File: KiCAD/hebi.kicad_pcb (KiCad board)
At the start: 4 copper layers, 49 x 49 mm, 111 parts, among them K1 CONN_3, K2 CONN_3, K3 CONN_3, K4 CONN_3, K5 CONN_3, P1 CONN_4, P2 CONN_4, P3 CONN_4, P4 CONN_4, P5 CONN_2, P6 CONN_2, Q1 MOS_N_DIODE, Q10 MOS_N_DIODE, Q2 MOS_N_DIODE, Q3 MOS_N_DIODE, Q4 MOS_N_DIODE, Q5 MOS_N_DIODE, Q6 MOS_N_DIODE, Q7 MOS_N_DIODE, Q8 MOS_N, Q9 MOS_N_DIODE, SW1 SW_PUSH, SW2 SW_PUSH, SW3 SW_PUSH, U1 MPU-6050, U2 HMC5883L, U3 MCP1825S, U4 STM32F407VG, U5 XBEE, U6 74AHC2G126, X1 8MHz

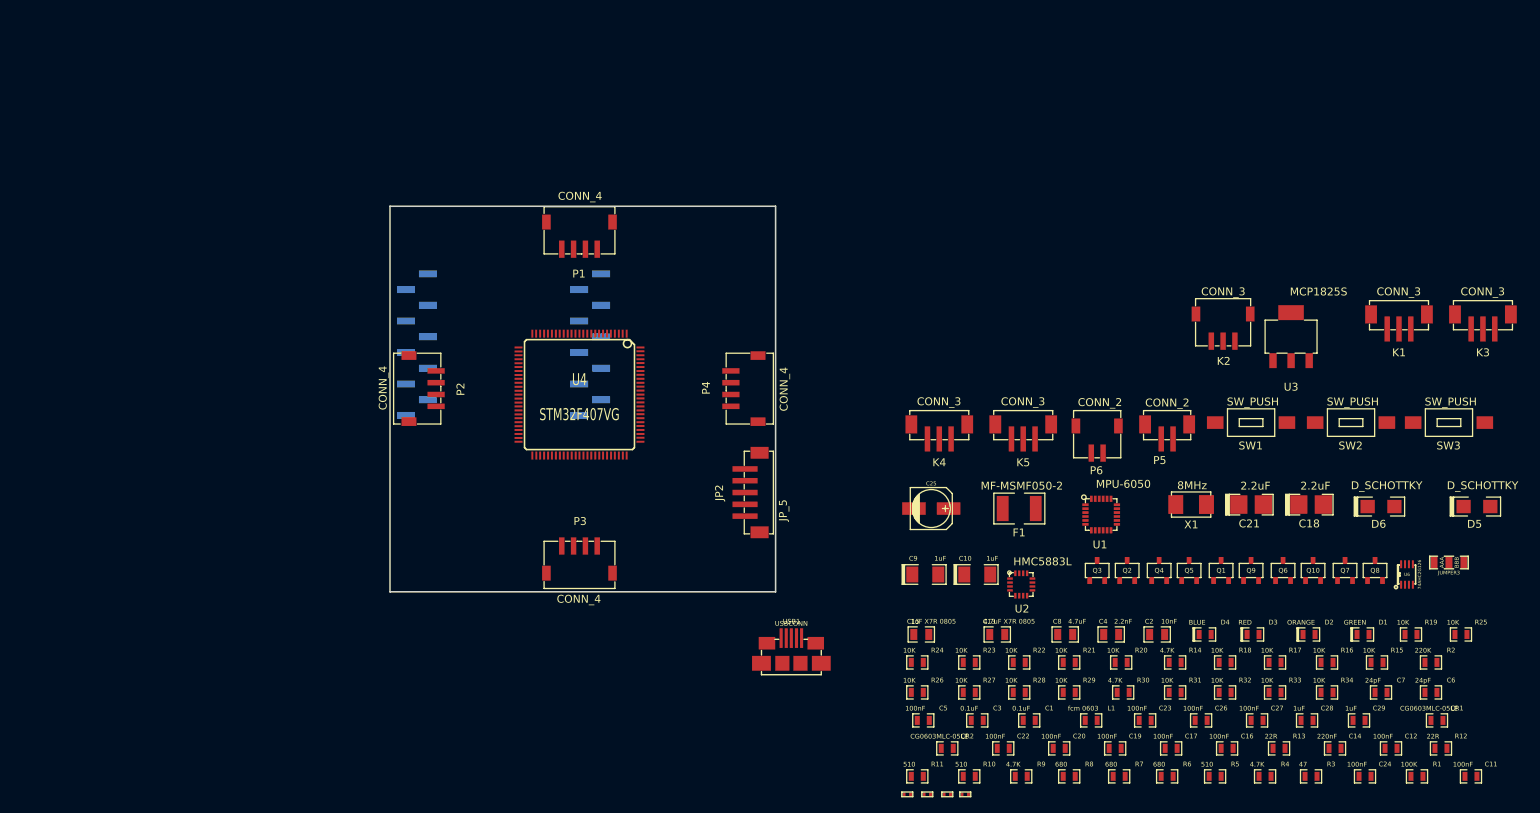
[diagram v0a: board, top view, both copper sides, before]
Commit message: Placed some components on the PCB.
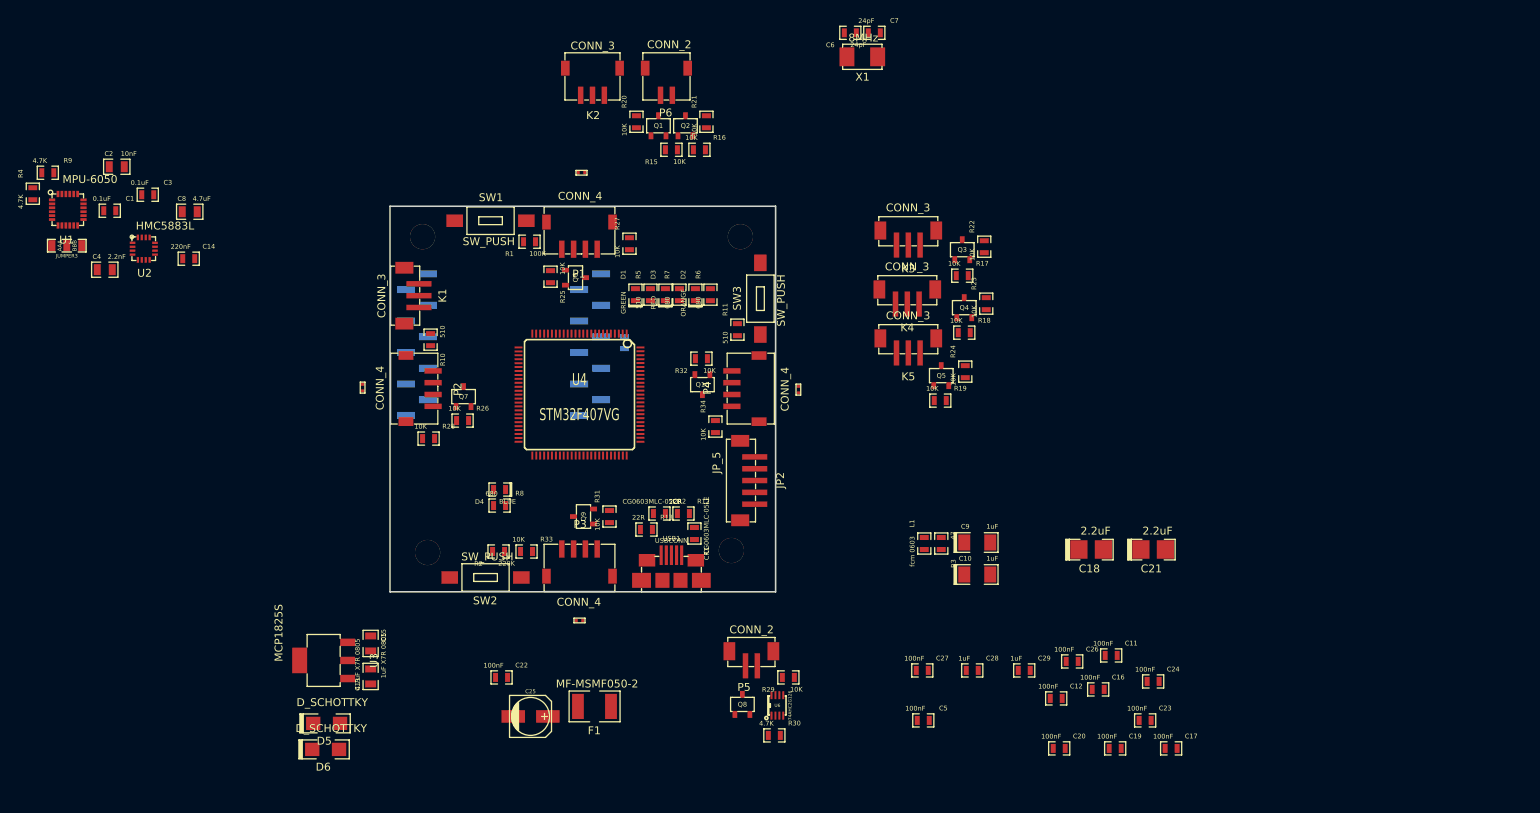
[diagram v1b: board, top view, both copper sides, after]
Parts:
- added Taladro3mm: 3mm, Taladro3mm, F.Cu at (178.6, 155.7)
- added Taladro3mm: 3mm, Taladro3mm, F.Cu at (217.2, 155.4)
- added Taladro3mm: 3mm, Taladro3mm, F.Cu at (177.9, 115.6)
- added Taladro3mm: 3mm, Taladro3mm, F.Cu at (218.3, 115.6)
- Q1, Q10, Q2, Q3, Q4, Q5, Q6, Q7, Q8, Q9: footprint SMT4dummies_SOT23-5_Opendous -> hebi_SOT23-3
- R14: moved to B.Cu
- moved JP1 180.2 mm to (132.7, 116.7)
- moved R4 173.2 mm to (128.4, 110.1), turned to 90 degrees
- moved C14 158.4 mm to (148.2, 118.4)
- moved D5 148.8 mm to (165.7, 177.4)
- moved R9 145.6 mm to (130.3, 107.4)
- moved C2 145.0 mm to (139.1, 106.7)
- moved D6 137.6 mm to (165.6, 180.7)
- moved U1 136.9 mm to (132.8, 112.1)
- moved C4 136.0 mm to (137.5, 119.8)
- moved C1 133.6 mm to (138.2, 112.3)
- moved R1 131.7 mm to (191.5, 116.2), turned to 180 degrees
- moved U3 129.6 mm to (165.4, 169.4), turned to 90 degrees
- moved K1 128.1 mm to (173.9, 123.1), turned to 90 degrees
- moved C3 124.8 mm to (143.0, 110.2)
- moved R25 124.3 mm to (194.2, 120.7), turned to 270 degrees
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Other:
- net class Thin added: clearance 0.254, trace_width 0.2, via_dia 0.889, via_drill 0.635
- rule trace_min: 0.254 -> 0.1524

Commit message: Placed more footprints on board.
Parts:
- K2, P6, Q1, Q2, R15, R16, R20, R21: moved to B.Cu
- moved R6 32.2 mm to (240.0, 142.6)
- moved D1 32.2 mm to (230.5, 142.6)
- moved D2 32.2 mm to (238.1, 142.6)
- moved D3 32.2 mm to (234.3, 142.6)
- moved R5 32.2 mm to (232.4, 142.6)
- moved R7 32.2 mm to (236.1, 142.6)
- moved R20 22.5 mm to (217.0, 120.0)
- moved R21 20.7 mm to (206.0, 120.0)
- moved Q1 20.0 mm to (214.1, 120.5), turned to 180 degrees
- moved R15 20.0 mm to (214.2, 124.0)
- moved K2 19.9 mm to (202.6, 111.9), turned to 180 degrees
- moved R16 19.9 mm to (209.0, 124.0), turned to 180 degrees
- moved P6 19.8 mm to (211.5, 111.9), turned to 180 degrees
- moved Q2 19.2 mm to (209.0, 120.5), turned to 180 degrees
- moved U5 13.7 mm to (198.1, 138.7)
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
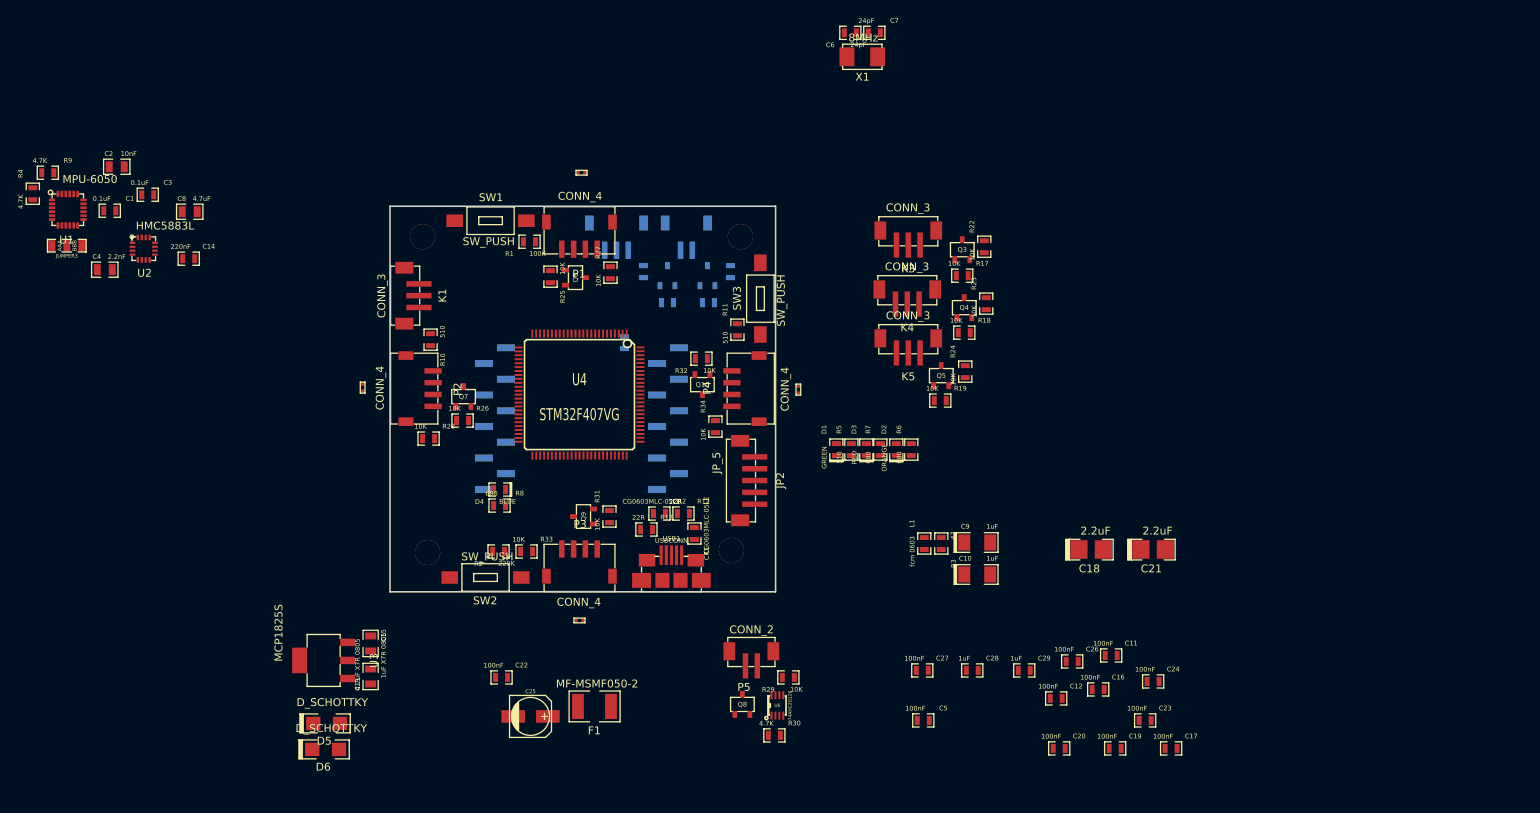
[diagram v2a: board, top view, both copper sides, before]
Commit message: Removed dynamixel due to spatial requirements (no space left for that)
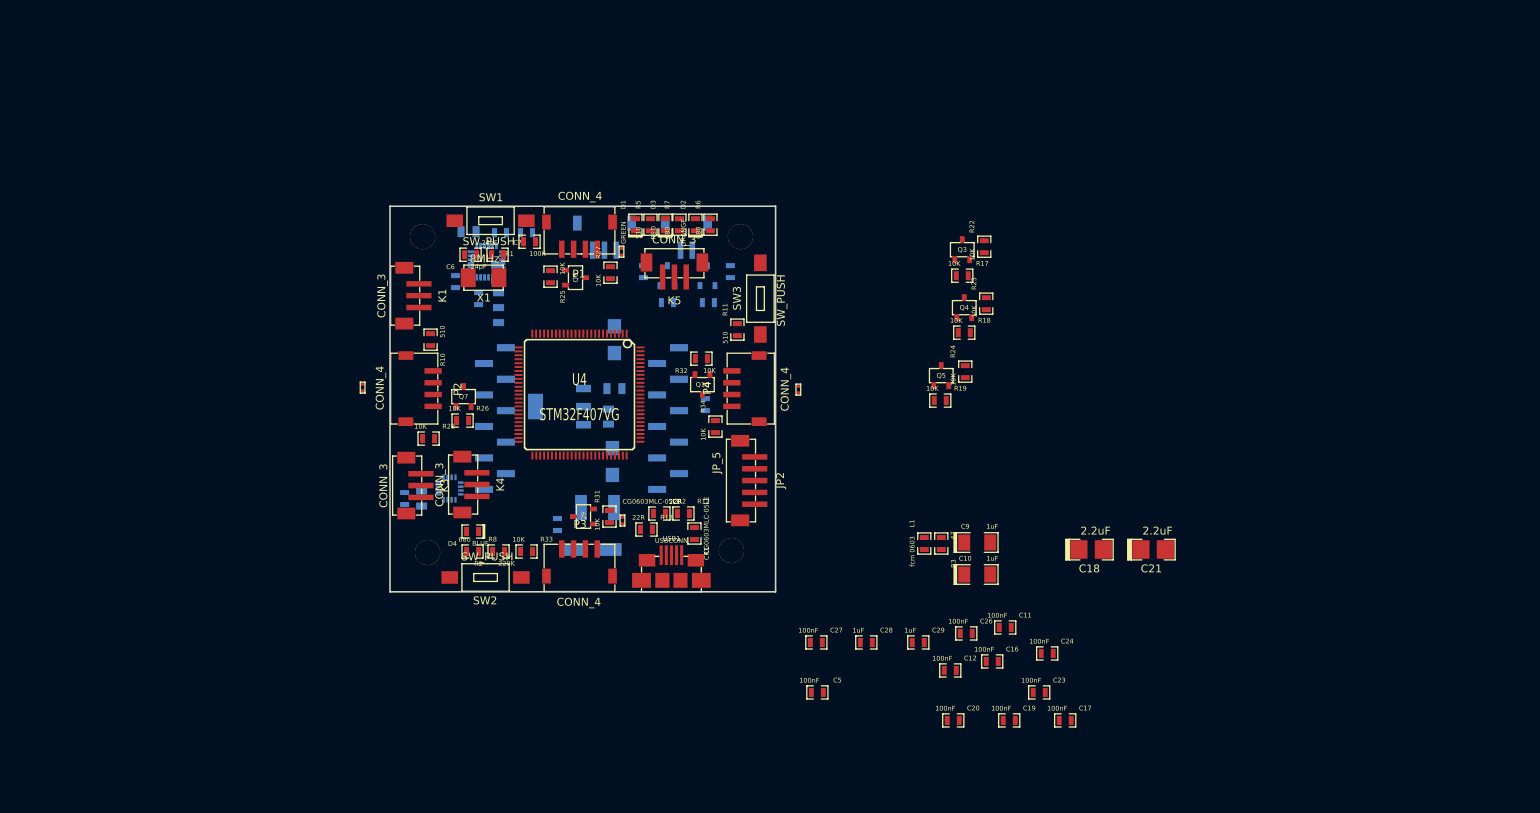
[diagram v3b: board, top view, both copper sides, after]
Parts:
- removed P5: CONN_2, ZH_CONN_B2B-ZR-SM4-TF
- removed Q8: MOS_N, hebi_SOT23-3
- removed R29: 10K, SM0603_Opendous(generic)
- removed R30: 4.7K, SM0603_Opendous(generic)
- removed U6: 74AHC2G126, VSSOP8_0.5mmPitch_2.3mm
- C1, C13, C14, C15, C2, C22, C25, C3, C4, C8, D5, D6, F1, JP1, R4, R9, U1, U2, U3: moved to B.Cu
- moved K3 73.9 mm to (174.1, 147.2), turned to 90 degrees
- moved K4 64.1 mm to (181.2, 147.1), turned to 90 degrees
- moved R4 62.9 mm to (191.1, 115.1), turned to 0 degrees
- moved D5 61.0 mm to (202.3, 128.7), turned to 90 degrees
- moved R9 58.0 mm to (187.8, 115.1), turned to 180 degrees
- moved C6 55.9 mm to (184.0, 117.9)
- moved X1 55.7 mm to (185.7, 120.8)
- moved C7 55.6 mm to (187.5, 117.9)
- moved JP1 55.4 mm to (187.6, 124.6), turned to 270 degrees
- moved U1 53.6 mm to (186.1, 118.7), turned to 180 degrees
- moved D6 51.6 mm to (202.1, 144.1), turned to 270 degrees
- moved C2 50.1 mm to (187.3, 120.1), turned to 90 degrees
- moved U2 49.4 mm to (181.4, 147.6), turned to 180 degrees
- moved C13 47.9 mm to (202.3, 134.9), turned to 0 degrees
- moved C8 46.9 mm to (177.8, 148.8), turned to 270 degrees
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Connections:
- U4 pad 80: /TX_DYN -> N-0000072
- U4 pad 82: /DIR_PORT_DYN -> N-0000070
- U4 pad 83: /RX_DYN -> N-0000071

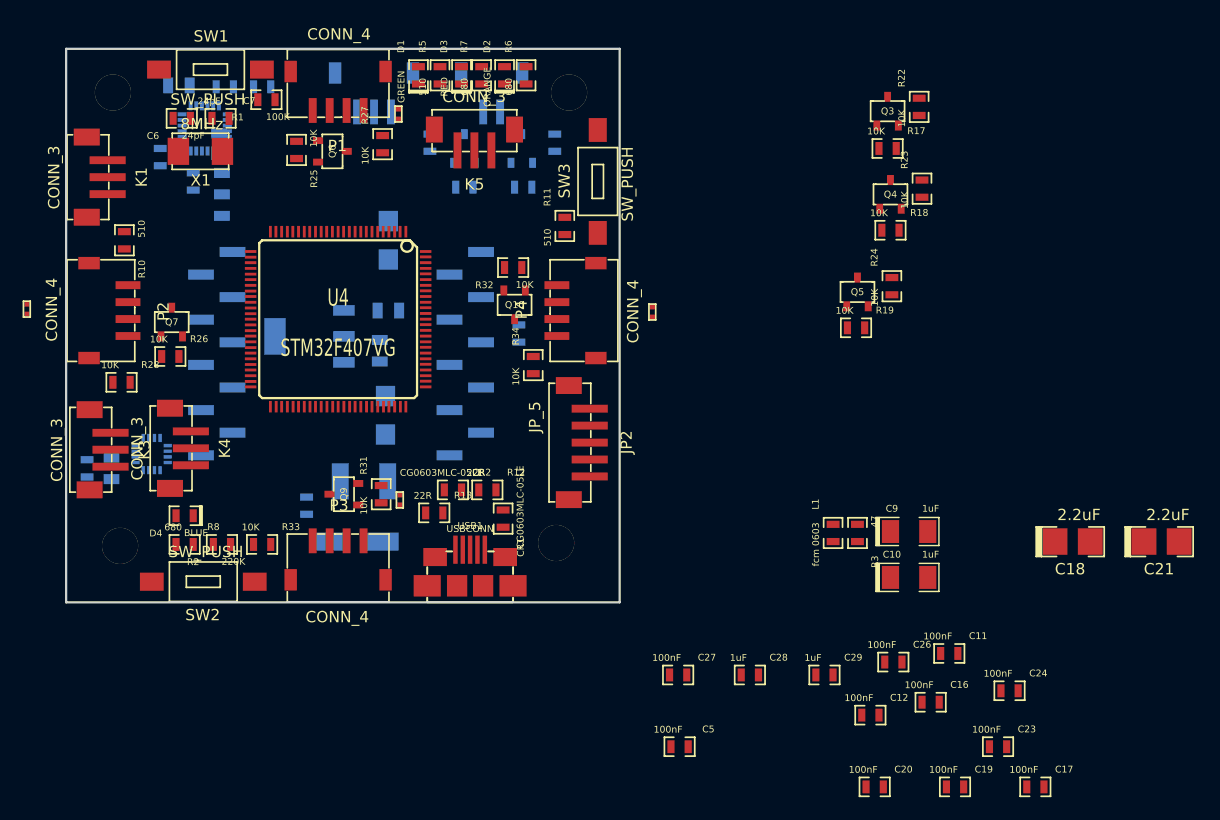
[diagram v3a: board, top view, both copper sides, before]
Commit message: Routed front layer (mostly, without vias)
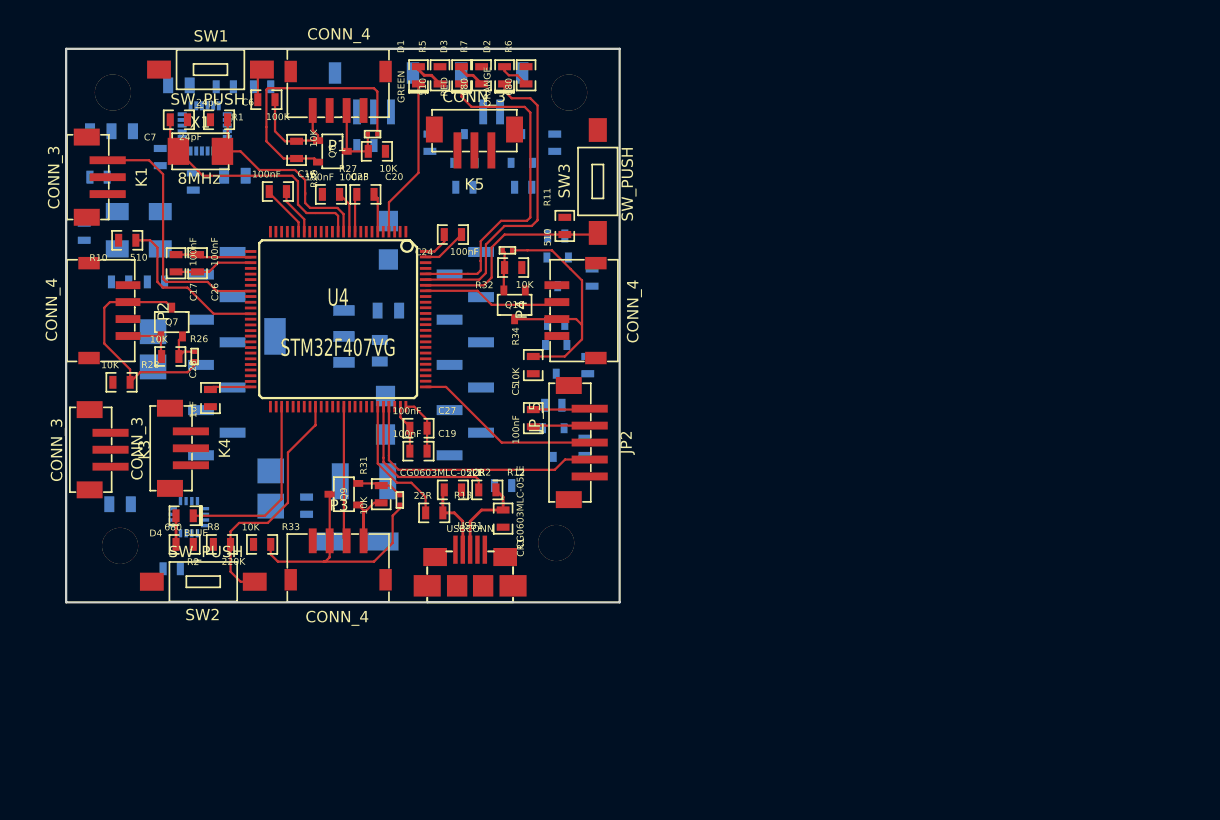
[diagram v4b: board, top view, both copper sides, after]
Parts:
- C10, C11, C12, C18, C21, C29, C9, L1, Q3, Q4, Q5, R17, R18, R19, R22, R23, R24, R3: moved to B.Cu
- moved C17 89.1 mm to (183.5, 130.7), turned to 270 degrees
- moved C11 85.2 mm to (175.4, 127.9), turned to 90 degrees
- moved C12 83.3 mm to (176.7, 123.1), turned to 180 degrees
- moved C18 83.2 mm to (181.5, 138.3), turned to 90 degrees
- moved C21 79.0 mm to (191.9, 150.6), turned to 270 degrees
- moved C23 76.7 mm to (197.2, 124.6)
- moved C9 75.0 mm to (178.3, 127.8), turned to 90 degrees
- moved C16 73.4 mm to (192.5, 124.3)
- moved C10 73.1 mm to (182.1, 127.8), turned to 90 degrees
- moved C26 71.0 mm to (185.4, 130.7), turned to 270 degrees
- moved C20 69.2 mm to (200.3, 124.6)
- moved L1 66.9 mm to (178.6, 132.3), turned to 0 degrees
- moved R3 66.0 mm to (181.7, 132.3), turned to 0 degrees
- moved C24 63.7 mm to (208.0, 128.1), turned to 180 degrees
- moved C29 62.0 mm to (200.3, 120.3), turned to 180 degrees
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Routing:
- net VCC: track 0.00 -> 52.3 mm
- net /LED3: track 0.00 -> 30.0 mm
- net GND: track 0.00 -> 28.0 mm
- net /LED2: track 0.00 -> 27.8 mm
- net /TX1_3V: track 0.00 -> 23.7 mm
- net /TX4: track 0.00 -> 23.6 mm
- net /SWDIO: track 0.00 -> 23.2 mm
- net /ADC3: track 0.00 -> 22.9 mm
- net /TX2: track 0.00 -> 22.6 mm
- net N-00000132: track 0.00 -> 22.2 mm
- net /PUSH_SW: track 0.00 -> 21.8 mm
- net /TX3: track 0.00 -> 20.6 mm
- net N-00000133: track 0.00 -> 18.9 mm
- net /BOOT0: track 0.00 -> 18.7 mm
- net /LED4: track 0.00 -> 16.6 mm
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
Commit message: Traced more traces.
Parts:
- moved C11 6.99 mm to (177.7, 134.5), turned to 180 degrees
- moved C13 5.21 mm to (198.8, 131.1), turned to 180 degrees
- moved D5 3.89 mm to (203.1, 124.8)
- moved C15 3.38 mm to (198.8, 140.3), turned to 180 degrees
- moved U3 3.35 mm to (198.4, 135.8)
- moved D6 2.87 mm to (200.0, 146.2), turned to 180 degrees
- moved C12 2.43 mm to (178.3, 121.3)
- moved JP1 1.66 mm to (179.5, 118.9)
- moved R14 0.92 mm to (211.6, 150.6)
- moved R24 0.38 mm to (220.7, 132.0)
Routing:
- net /SERVO_PWR: track 0.00 -> 106.7 mm, vias 0 -> 4
- net /SERVO1_5V: track 0.00 -> 65.4 mm, vias 0 -> 1
- net /SERVO2_5V: track 0.00 -> 60.0 mm, vias 0 -> 1
- net /SERVO3_3V: track 0.00 -> 54.8 mm, vias 0 -> 3
- net /I2C_SDA_PWR_3V: track 0.00 -> 34.3 mm, vias 0 -> 1
- net +5V: track 0.00 -> 32.6 mm
- net VCC: track 52.3 -> 84.0 mm
- net /ADC1: track 0.00 -> 29.4 mm, vias 0 -> 2
- net /I2C_SCL_PWR_3V: track 0.00 -> 26.1 mm, vias 0 -> 1
- net /RESET: track 7.86 -> 33.4 mm, vias 0 -> 2
- net /XBEE_RX: track 0.00 -> 25.0 mm, vias 0 -> 1
- net /XBEE_TX: track 0.00 -> 24.9 mm, vias 0 -> 1
- net /ADC2: track 0.00 -> 24.2 mm, vias 0 -> 2
- net N-0000046: track 0.00 -> 23.1 mm
- net /RX3: track 0.00 -> 23.0 mm, vias 0 -> 2
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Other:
- net class Thick added: clearance 0.254, trace_width 0.635, via_dia 0.889, via_drill 0.635
- net class Thin: trace_width 0.2 -> 0.203
